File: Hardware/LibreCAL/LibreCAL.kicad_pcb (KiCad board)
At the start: 4 copper layers, 55 x 73.5 mm, 132 parts, among them J1 901-10510-2, J2 901-10510-2, J3 901-10510-2, J4 901-10510-2, J5 USB_C_Receptacle_USB2.0, J6 TC2030-ARM, Q1 IRLML2060, SW1 TL3301NF160QG, SW2 TL3301CF160QG, SW3 TL3301CF160QG, U1 PE426462, U2 PE426462, U3 PE426462, U4 PE426462, U5 W25Q16JVSNIQ, U6 IP4234CZ6, U7 RP2040, U8 W25Q128JVSIQ, U9 MIC5528-3.3YMT-TR, Y1 ECS-120-8-36-CKM-TR3

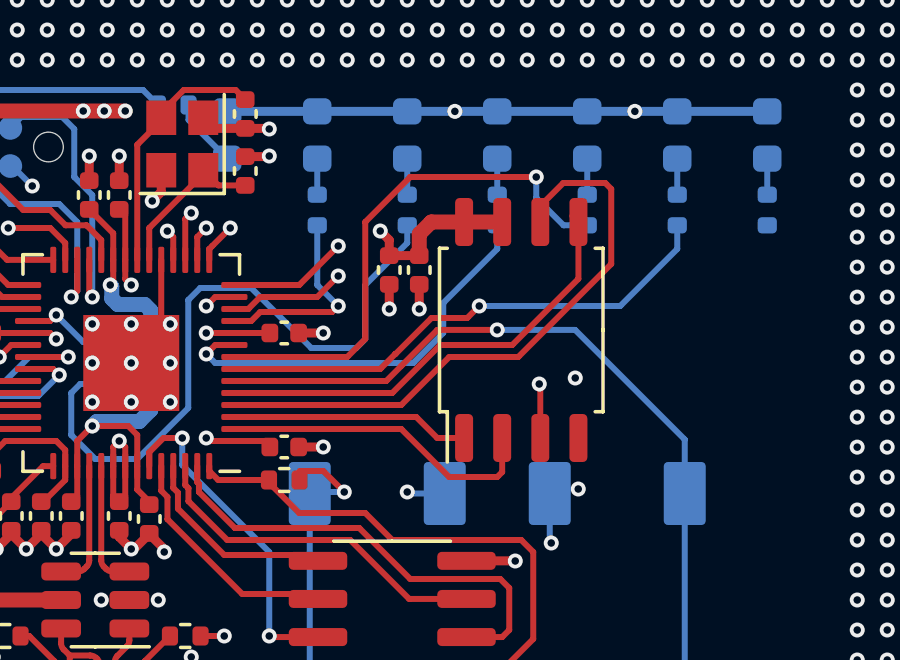
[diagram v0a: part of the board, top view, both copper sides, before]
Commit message: Switch to W25N01GVZEIG 1Gbit flash
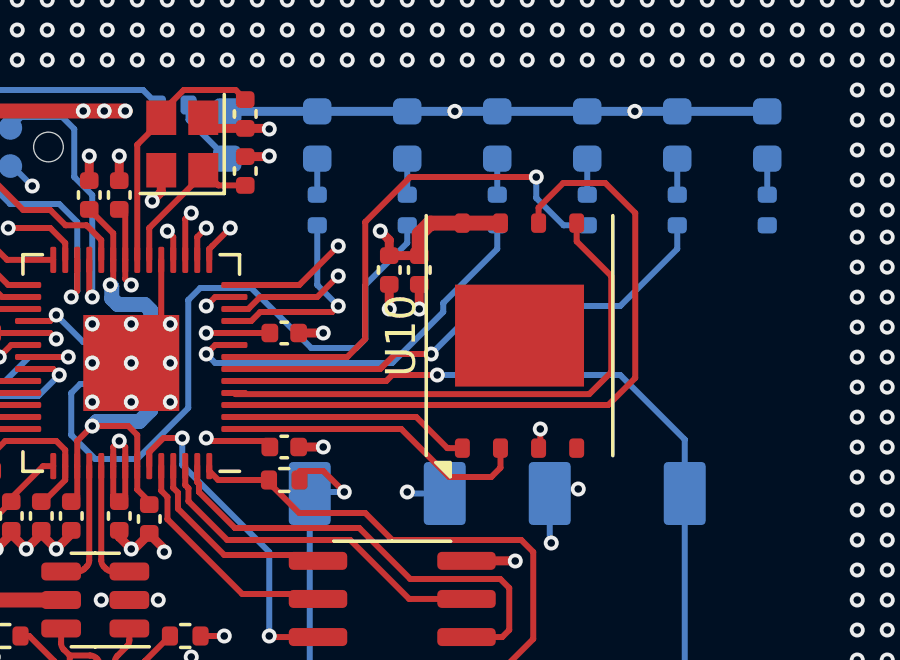
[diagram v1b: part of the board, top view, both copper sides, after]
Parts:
- removed U8: W25Q128JVSIQ, Package_SO:SOIC-8_5.23x5.23mm_P1.27mm
- added U10: W25N01GVZEIG, Package_SON:WSON-8-1EP_8x6mm_P1.27mm_EP3.4x4.3mm, F.Cu at (141.7, 119.7)
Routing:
- net Net-(U10-CLK): track 20.3 -> 23.7 mm
- net Net-(U10-DI(IO_{0})): track 15.1 -> 18.3 mm
- net +3V3: track 71.0 -> 69.4 mm
- net BUTTON1: track 28.1 -> 26.9 mm
- net GND: vias 1077 -> 1076

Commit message: Tweaks
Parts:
- moved U10 1.82 mm to (143.5, 119.2)
- moved C26 1.24 mm to (139.6, 117.2)
- moved C25 1.14 mm to (138.5, 117.2)
- moved C16 0.42 mm to (134.2, 119.3)
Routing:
- net +3V3: track 69.4 -> 74.1 mm
- net LED_WAIT: track 17.6 -> 13.6 mm
- net Net-(U10-DI(IO_{0})): track 18.3 -> 21.1 mm
- net Net-(U10-DO(IO_{1})): track 10.3 -> 12.0 mm
- net Net-(U10-~{CS}): track 8.03 -> 9.59 mm
- net Net-(U10-CLK): track 23.7 -> 25.2 mm
- net BUTTON1: track 26.9 -> 26.0 mm
- net LED_PORT1: track 13.4 -> 14.0 mm
- net GND: track 185.6 -> 185.2 mm, vias 1076 -> 1078
